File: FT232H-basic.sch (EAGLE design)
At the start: 26 parts, among them IC1 FT232H

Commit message: minor updates to board legend; added BOM files and board PDF
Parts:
- added FRAME1: FRAME-LETTER, SparkFun-Aesthetics:FRAME-LETTER
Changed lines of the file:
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@@
 <part name="C1" library="SparkFun-Passives" deviceset="CAP" device="0603-CAP" value="0.1uF"/>
 <part name="GND13" library="SparkFun-Aesthetics" deviceset="GND" device=""/>
+<part name="FRAME1" library="SparkFun-Aesthetics" deviceset="FRAME-LETTER" device=""/>
 </parts>
 <sheets>
@@
 <instance part="C1" gate="G$1" x="48.26" y="22.86"/>
 <instance part="GND13" gate="1" x="48.26" y="17.78"/>
+<instance part="FRAME1" gate="G$1" x="-0.254" y="-0.508"/>
+<instance part="FRAME1" gate="G$2" x="147.066" y="-0.508"/>
 </instances>
 <busses>

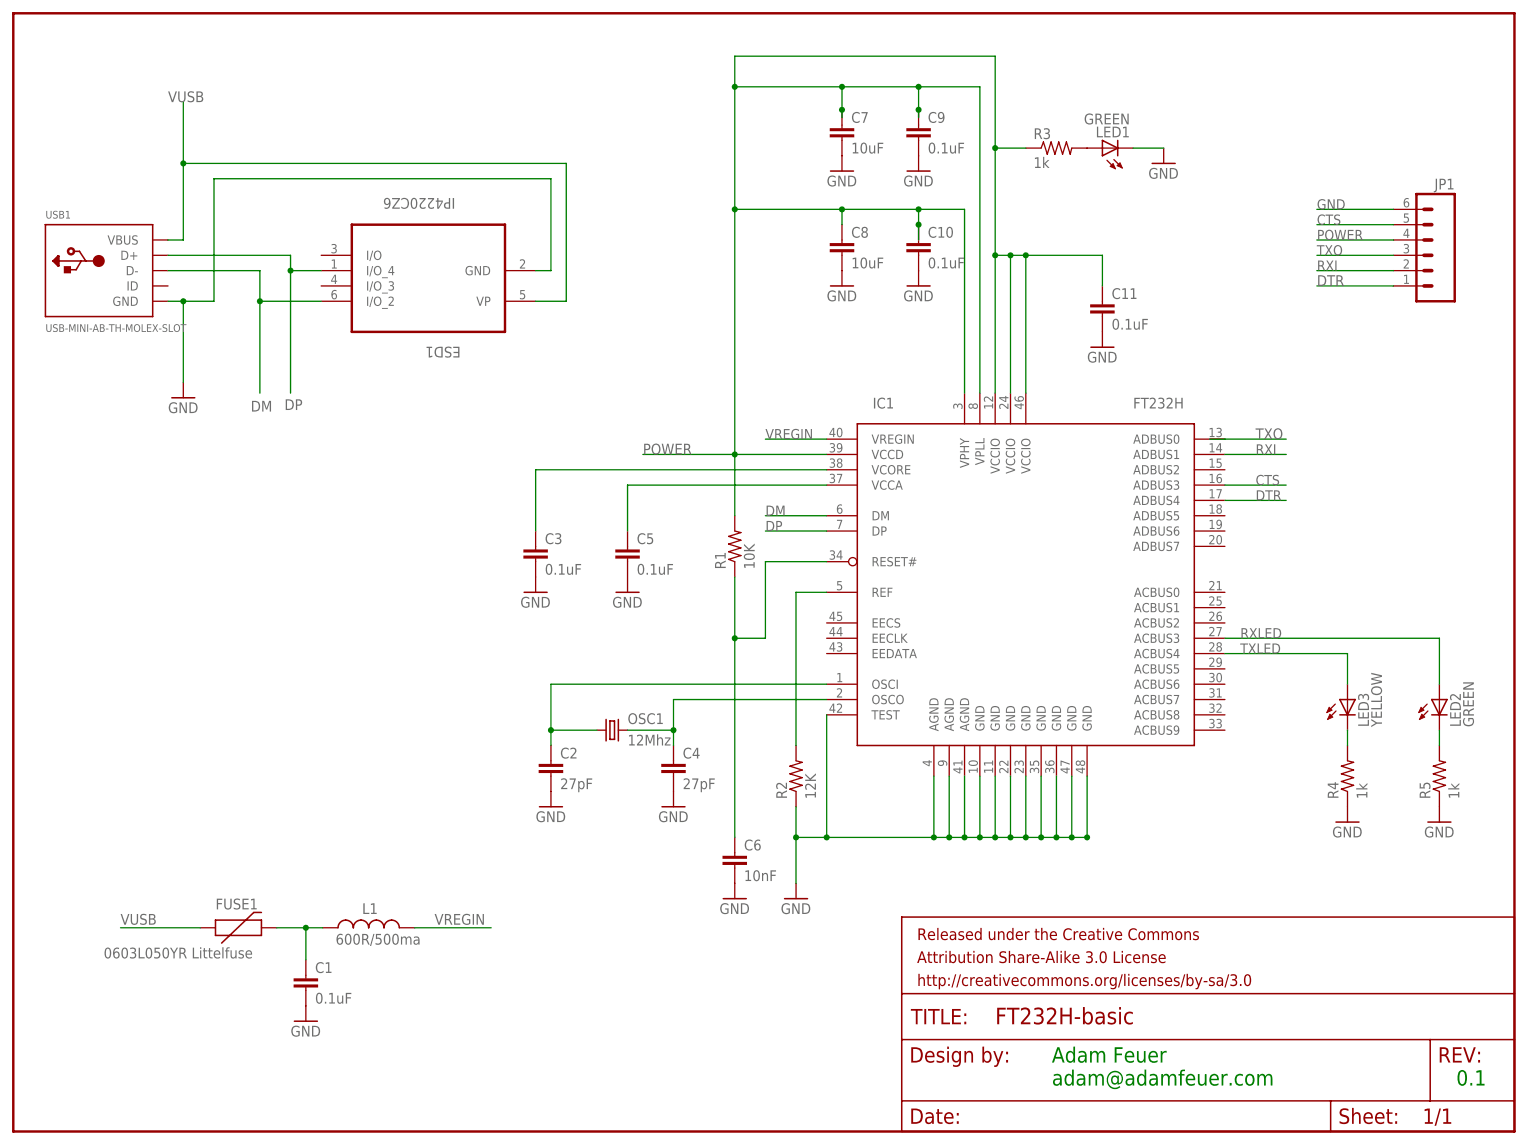
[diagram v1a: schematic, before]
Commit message: fixed TX/RX led bug - TX/RX signals are active low, so need to be connected to power via 47O ohm resistor, as per UM232H datasheet
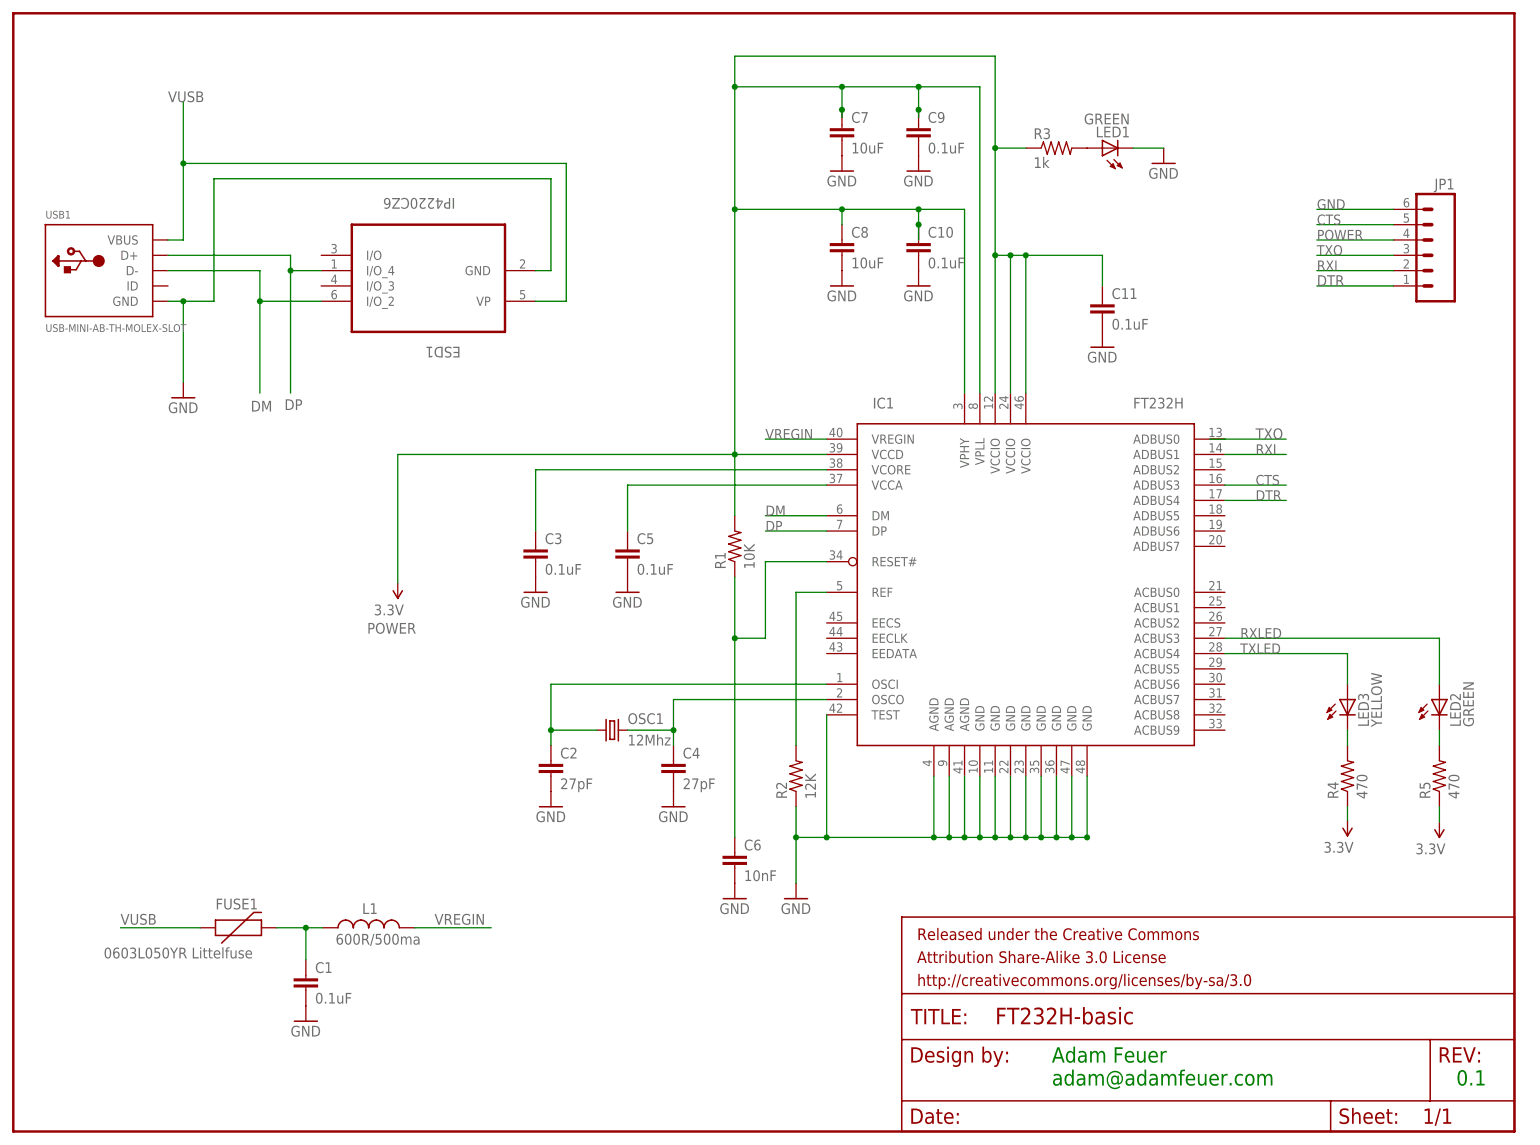
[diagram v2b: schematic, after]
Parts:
- R4, R5: value 1k -> 470
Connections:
- net GND: no longer R4.1, R5.1
- net POWER: now also R4.1, R5.1
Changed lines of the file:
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@@
 <part name="LED2" library="SparkFun-LED" deviceset="LED-GREEN" device="0603" value="GREEN"/>
 <part name="LED3" library="SparkFun-LED" deviceset="LED-YELLOW" device="0603" value="YELLOW"/>
-<part name="R4" library="SparkFun-Resistors" deviceset="1K-1%" device="" value="1k"/>
-<part name="R5" library="SparkFun-Resistors" deviceset="1K-1%" device="" value="1k"/>
-<part name="GND16" library="SparkFun-Aesthetics" deviceset="GND" device=""/>
-<part name="GND17" library="SparkFun-Aesthetics" deviceset="GND" device=""/>
+<part name="R4" library="SparkFun-Resistors" deviceset="1K-1%" device="" value="470"/>
+<part name="R5" library="SparkFun-Resistors" deviceset="1K-1%" device="" value="470"/>
 <part name="LED1" library="SparkFun-LED" deviceset="LED-GREEN" device="0603" value="GREEN"/>
 <part name="OSC1" library="SparkFun-FreqCtrl" deviceset="CRYSTAL" device="5X3" value="12Mhz"/>
@@
 <part name="GND13" library="SparkFun-Aesthetics" deviceset="GND" device=""/>
 <part name="FRAME1" library="SparkFun-Aesthetics" deviceset="FRAME-LETTER" device=""/>
+<part name="POWER" library="SparkFun-Aesthetics" deviceset="3.3V" device=""/>
+<part name="POWER1" library="SparkFun-Aesthetics" deviceset="3.3V" device=""/>
+<part name="POWER2" library="SparkFun-Aesthetics" deviceset="3.3V" device=""/>
 </parts>
 <sheets>
@@
 <instance part="R4" gate="G$1" x="220.98" y="58.42" rot="R90"/>
 <instance part="R5" gate="G$1" x="236.22" y="58.42" rot="R90"/>
-<instance part="GND16" gate="1" x="220.98" y="50.8"/>
-<instance part="GND17" gate="1" x="236.22" y="50.8"/>
 <instance part="LED1" gate="G$1" x="180.34" y="162.56" rot="R90"/>
 <instance part="OSC1" gate="G$1" x="99.06" y="66.04"/>
@@
 <instance part="FRAME1" gate="G$1" x="-0.254" y="-0.508"/>
 <instance part="FRAME1" gate="G$2" x="147.066" y="-0.508"/>
+<instance part="POWER" gate="G$1" x="63.5" y="90.424" rot="R180"/>
+<instance part="POWER1" gate="G$1" x="220.98" y="51.054" rot="R180"/>
+<instance part="POWER2" gate="G$1" x="236.22" y="50.8" rot="R180"/>
 </instances>
 <busses>
@@
 </segment>
 <segment>
-<pinref part="R4" gate="G$1" pin="1"/>
-<pinref part="GND16" gate="1" pin="GND"/>
-</segment>
-<segment>
-<pinref part="R5" gate="G$1" pin="1"/>
-<pinref part="GND17" gate="1" pin="GND"/>
-</segment>
-<segment>
 <pinref part="C1" gate="G$1" pin="2"/>
 <pinref part="GND13" gate="1" pin="GND"/>
@@
 <pinref part="C9" gate="G$1" pin="1"/>
 <junction x="149.86" y="168.91"/>
-<wire x1="119.38" y1="111.76" x2="104.14" y2="111.76" width="0.1524" layer="91"/>
-<label x="104.14" y="111.76" size="1.778" layer="95"/>
 <junction x="119.38" y="172.72"/>
 <junction x="119.38" y="152.4"/>
@@
 <pinref part="IC1" gate="G$1" pin="VPHY"/>
 <wire x1="157.48" y1="121.92" x2="157.48" y2="152.4" width="0.1524" layer="91"/>
-</segment>
-</net>
+<wire x1="119.38" y1="111.76" x2="63.5" y2="111.76" width="0.1524" layer="91"/>
+<wire x1="63.5" y1="111.76" x2="63.5" y2="90.424" width="0.1524" layer="91"/>
+<pinref part="POWER" gate="G$1" pin="3.3V"/>
+<label x="66.548" y="83.82" size="1.778" layer="95" rot="R180"/>
+</segment>
+<segment>
+<pinref part="R4" gate="G$1" pin="1"/>
+<wire x1="220.98" y1="53.34" x2="220.98" y2="51.054" width="0.1524" layer="91"/>
+<pinref part="POWER1" gate="G$1" pin="3.3V"/>
+</segment>
+<segment>
+<pinref part="R5" gate="G$1" pin="1"/>
+<wire x1="236.22" y1="53.34" x2="236.22" y2="50.8" width="0.1524" layer="91"/>
+<pinref part="POWER2" gate="G$1" pin="3.3V"/>
+</segment>
+</net>

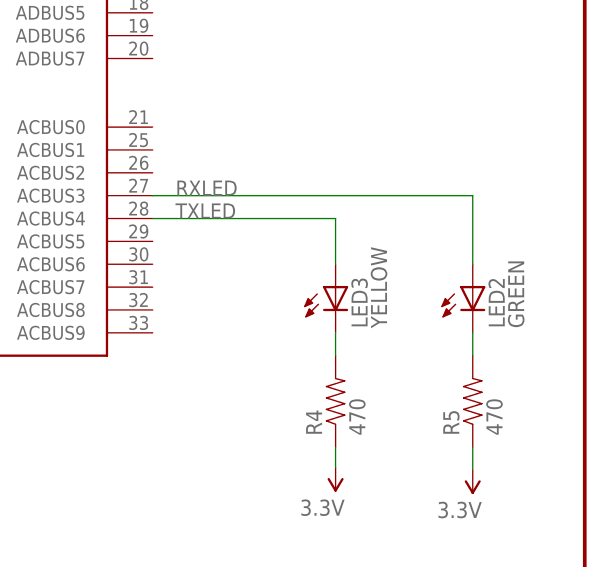
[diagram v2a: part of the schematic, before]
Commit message: fixed LED orientation - anode faces power
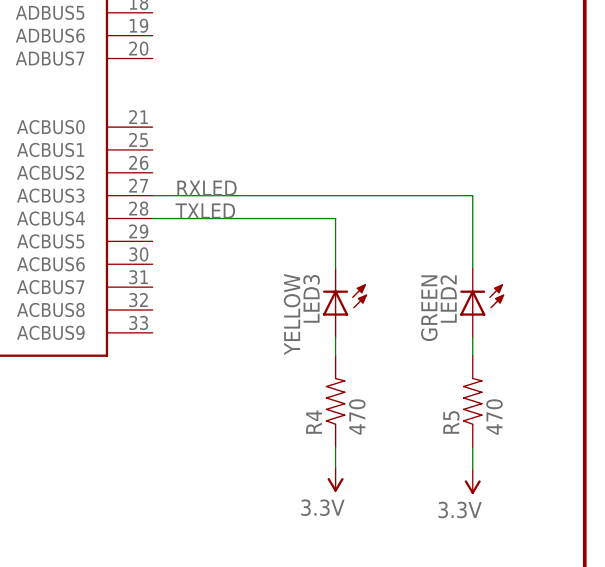
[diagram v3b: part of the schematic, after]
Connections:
- removed net N$11: LED2.C, R5.2
- new net N$8: LED3.A, R4.2
- net N$10: now also LED2.A, R5.2; no longer LED3.C, R4.2
- net RXLED: now also LED2.C; no longer LED2.A
- net TXLED: now also LED3.C; no longer LED3.A
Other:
- moved on the sheet: LED2, LED3
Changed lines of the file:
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@@
 <instance part="USB1" gate="G$1" x="15.24" y="142.24"/>
 <instance part="GND14" gate="1" x="27.94" y="121.158"/>
-<instance part="LED2" gate="G$1" x="236.22" y="71.12"/>
-<instance part="LED3" gate="G$1" x="220.98" y="71.12"/>
+<instance part="LED2" gate="G$1" x="236.22" y="68.072" rot="R180"/>
+<instance part="LED3" gate="G$1" x="220.98" y="68.072" rot="R180"/>
 <instance part="R4" gate="G$1" x="220.98" y="58.42" rot="R90"/>
 <instance part="R5" gate="G$1" x="236.22" y="58.42" rot="R90"/>
@@
 <pinref part="IC1" gate="G$1" pin="ACBUS3"/>
 <label x="203.2" y="81.28" size="1.6764" layer="95"/>
-<pinref part="LED2" gate="G$1" pin="A"/>
 <wire x1="200.66" y1="81.28" x2="236.22" y2="81.28" width="0.1524" layer="91"/>
-<wire x1="236.22" y1="81.28" x2="236.22" y2="73.66" width="0.1524" layer="91"/>
+<pinref part="LED2" gate="G$1" pin="C"/>
+<wire x1="236.22" y1="73.152" x2="236.22" y2="81.28" width="0.1524" layer="91"/>
 </segment>
 </net>
@@
 <pinref part="IC1" gate="G$1" pin="ACBUS4"/>
 <label x="203.2" y="78.74" size="1.6764" layer="95"/>
-<pinref part="LED3" gate="G$1" pin="A"/>
 <wire x1="200.66" y1="78.74" x2="220.98" y2="78.74" width="0.1524" layer="91"/>
-<wire x1="220.98" y1="78.74" x2="220.98" y2="73.66" width="0.1524" layer="91"/>
-</segment>
-</net>
-<net name="N$10" class="0">
-<segment>
 <pinref part="LED3" gate="G$1" pin="C"/>
-<pinref part="R4" gate="G$1" pin="2"/>
-<wire x1="220.98" y1="66.04" x2="220.98" y2="63.5" width="0.1524" layer="91"/>
-</segment>
-</net>
-<net name="N$11" class="0">
-<segment>
-<pinref part="LED2" gate="G$1" pin="C"/>
-<pinref part="R5" gate="G$1" pin="2"/>
-<wire x1="236.22" y1="66.04" x2="236.22" y2="63.5" width="0.1524" layer="91"/>
+<wire x1="220.98" y1="73.152" x2="220.98" y2="78.74" width="0.1524" layer="91"/>
 </segment>
 </net>
@@
 </segment>
 </net>
+<net name="N$10" class="0">
+<segment>
+<pinref part="R5" gate="G$1" pin="2"/>
+<pinref part="LED2" gate="G$1" pin="A"/>
+<wire x1="236.22" y1="63.5" x2="236.22" y2="65.532" width="0.1524" layer="91"/>
+</segment>
+</net>
+<net name="N$8" class="0">
+<segment>
+<pinref part="LED3" gate="G$1" pin="A"/>
+<pinref part="R4" gate="G$1" pin="2"/>
+<wire x1="220.98" y1="65.532" x2="220.98" y2="63.5" width="0.1524" layer="91"/>
+</segment>
+</net>

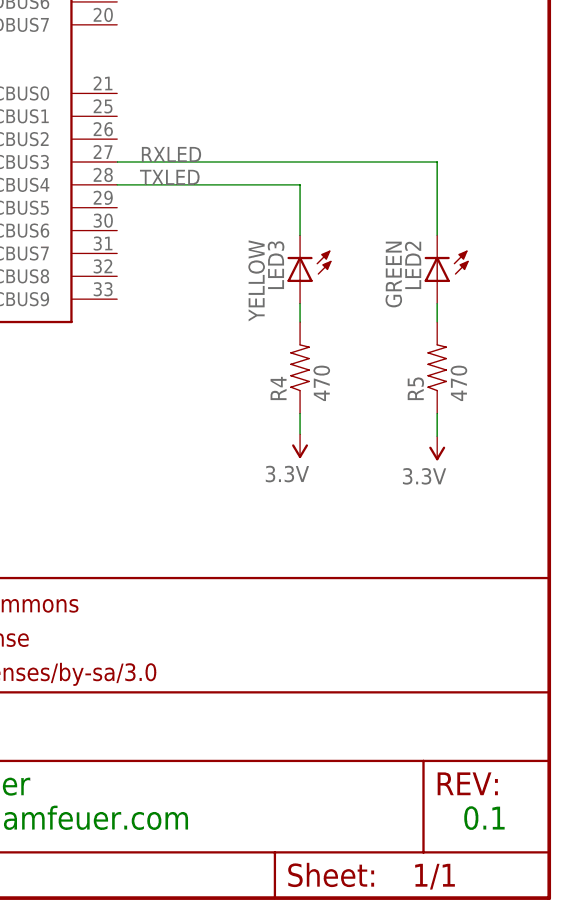
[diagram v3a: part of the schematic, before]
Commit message: corrected RX and TX LED circuit
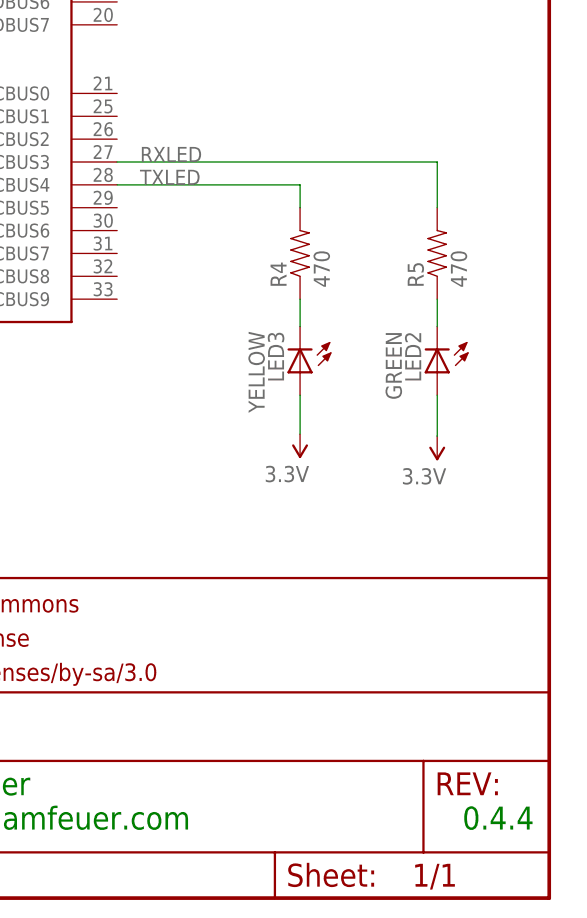
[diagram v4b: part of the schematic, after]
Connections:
- net N$10: now also LED2.C, R5.1; no longer LED2.A, R5.2
- net N$8: now also LED3.C, R4.1; no longer LED3.A, R4.2
- net POWER: now also LED2.A, LED3.A; no longer R4.1, R5.1
- net RXLED: now also R5.2; no longer LED2.C
- net TXLED: now also R4.2; no longer LED3.C
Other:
- note added: "0.4.4"
- note removed: "0.1"
- moved on the sheet: LED2, LED3, R4, R5
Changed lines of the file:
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@@
 <text x="171.958" y="7.112" size="2.54" layer="91">Adam Feuer
 adam@adamfeuer.com</text>
-<text x="239.014" y="7.112" size="2.54" layer="91">0.1</text>
+<text x="239.014" y="7.112" size="2.54" layer="91">0.4.4</text>
 </plain>
 <instances>
@@
 <instance part="USB1" gate="G$1" x="15.24" y="142.24"/>
 <instance part="GND14" gate="1" x="27.94" y="121.158"/>
-<instance part="LED2" gate="G$1" x="236.22" y="68.072" rot="R180"/>
-<instance part="LED3" gate="G$1" x="220.98" y="68.072" rot="R180"/>
-<instance part="R4" gate="G$1" x="220.98" y="58.42" rot="R90"/>
-<instance part="R5" gate="G$1" x="236.22" y="58.42" rot="R90"/>
+<instance part="LED2" gate="G$1" x="236.22" y="57.912" rot="R180"/>
+<instance part="LED3" gate="G$1" x="220.98" y="57.912" rot="R180"/>
+<instance part="R4" gate="G$1" x="220.98" y="71.12" rot="R90"/>
+<instance part="R5" gate="G$1" x="236.22" y="71.12" rot="R90"/>
 <instance part="LED1" gate="G$1" x="180.34" y="162.56" rot="R90"/>
 <instance part="OSC1" gate="G$1" x="99.06" y="66.04"/>
@@
 </segment>
 <segment>
-<pinref part="R4" gate="G$1" pin="1"/>
-<wire x1="220.98" y1="53.34" x2="220.98" y2="51.054" width="0.1524" layer="91"/>
+<pinref part="LED3" gate="G$1" pin="A"/>
 <pinref part="POWER1" gate="G$1" pin="3.3V"/>
-</segment>
-<segment>
-<pinref part="R5" gate="G$1" pin="1"/>
-<wire x1="236.22" y1="53.34" x2="236.22" y2="50.8" width="0.1524" layer="91"/>
+<wire x1="220.98" y1="55.372" x2="220.98" y2="51.054" width="0.1524" layer="91"/>
+</segment>
+<segment>
+<pinref part="LED2" gate="G$1" pin="A"/>
 <pinref part="POWER2" gate="G$1" pin="3.3V"/>
+<wire x1="236.22" y1="55.372" x2="236.22" y2="50.8" width="0.1524" layer="91"/>
 </segment>
 </net>
@@
 <label x="203.2" y="81.28" size="1.6764" layer="95"/>
 <wire x1="200.66" y1="81.28" x2="236.22" y2="81.28" width="0.1524" layer="91"/>
-<pinref part="LED2" gate="G$1" pin="C"/>
-<wire x1="236.22" y1="73.152" x2="236.22" y2="81.28" width="0.1524" layer="91"/>
+<pinref part="R5" gate="G$1" pin="2"/>
+<wire x1="236.22" y1="81.28" x2="236.22" y2="76.2" width="0.1524" layer="91"/>
 </segment>
 </net>
@@
 <label x="203.2" y="78.74" size="1.6764" layer="95"/>
 <wire x1="200.66" y1="78.74" x2="220.98" y2="78.74" width="0.1524" layer="91"/>
-<pinref part="LED3" gate="G$1" pin="C"/>
-<wire x1="220.98" y1="73.152" x2="220.98" y2="78.74" width="0.1524" layer="91"/>
+<pinref part="R4" gate="G$1" pin="2"/>
+<wire x1="220.98" y1="78.74" x2="220.98" y2="76.2" width="0.1524" layer="91"/>
 </segment>
 </net>
@@
 </segment>
 </net>
+<net name="N$8" class="0">
+<segment>
+<pinref part="R4" gate="G$1" pin="1"/>
+<pinref part="LED3" gate="G$1" pin="C"/>
+<wire x1="220.98" y1="66.04" x2="220.98" y2="62.992" width="0.1524" layer="91"/>
+</segment>
+</net>
 <net name="N$10" class="0">
 <segment>
-<pinref part="R5" gate="G$1" pin="2"/>
-<pinref part="LED2" gate="G$1" pin="A"/>
-<wire x1="236.22" y1="63.5" x2="236.22" y2="65.532" width="0.1524" layer="91"/>
-</segment>
-</net>
-<net name="N$8" class="0">
-<segment>
-<pinref part="LED3" gate="G$1" pin="A"/>
-<pinref part="R4" gate="G$1" pin="2"/>
-<wire x1="220.98" y1="65.532" x2="220.98" y2="63.5" width="0.1524" layer="91"/>
-</segment>
-</net>
+<pinref part="R5" gate="G$1" pin="1"/>
+<pinref part="LED2" gate="G$1" pin="C"/>
+<wire x1="236.22" y1="66.04" x2="236.22" y2="62.992" width="0.1524" layer="91"/>
+</segment>
+</net>
